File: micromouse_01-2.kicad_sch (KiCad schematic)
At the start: 50 parts, among them IC6 PCA9632TK,118, J1 Conn_01x02, M3 Fan_Motor, Q1 MCM3400A-TP, Q2 MCM3400A-TP, Q3 MCM3400A-TP, Q4 SSM6J808R_LXHF, SW1 SSSS810701, U1 SMT-0440-S-R, U2 LBR-127HLD, U3 LBR-127HLD, U4 LBR-127HLD, U5 LBR-127HLD, U6 LXDC55FAAA-203

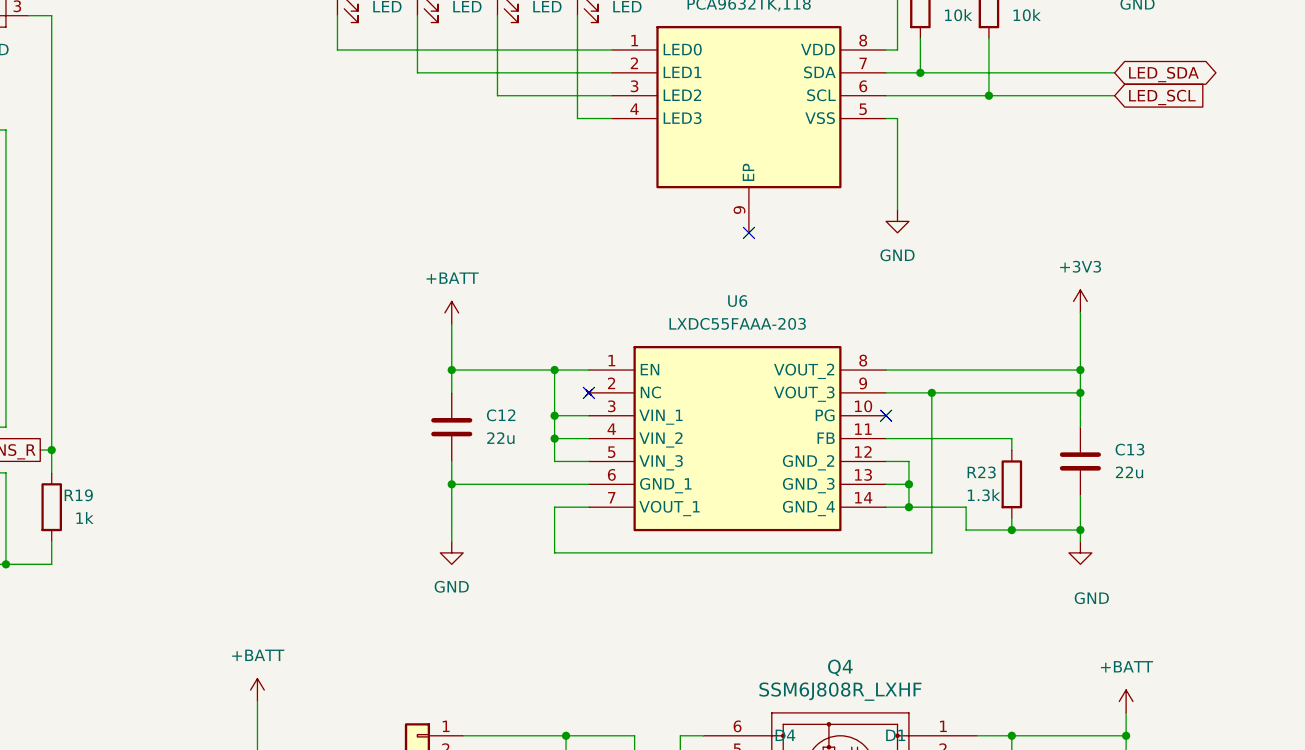
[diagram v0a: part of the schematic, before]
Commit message: [add]LED追加
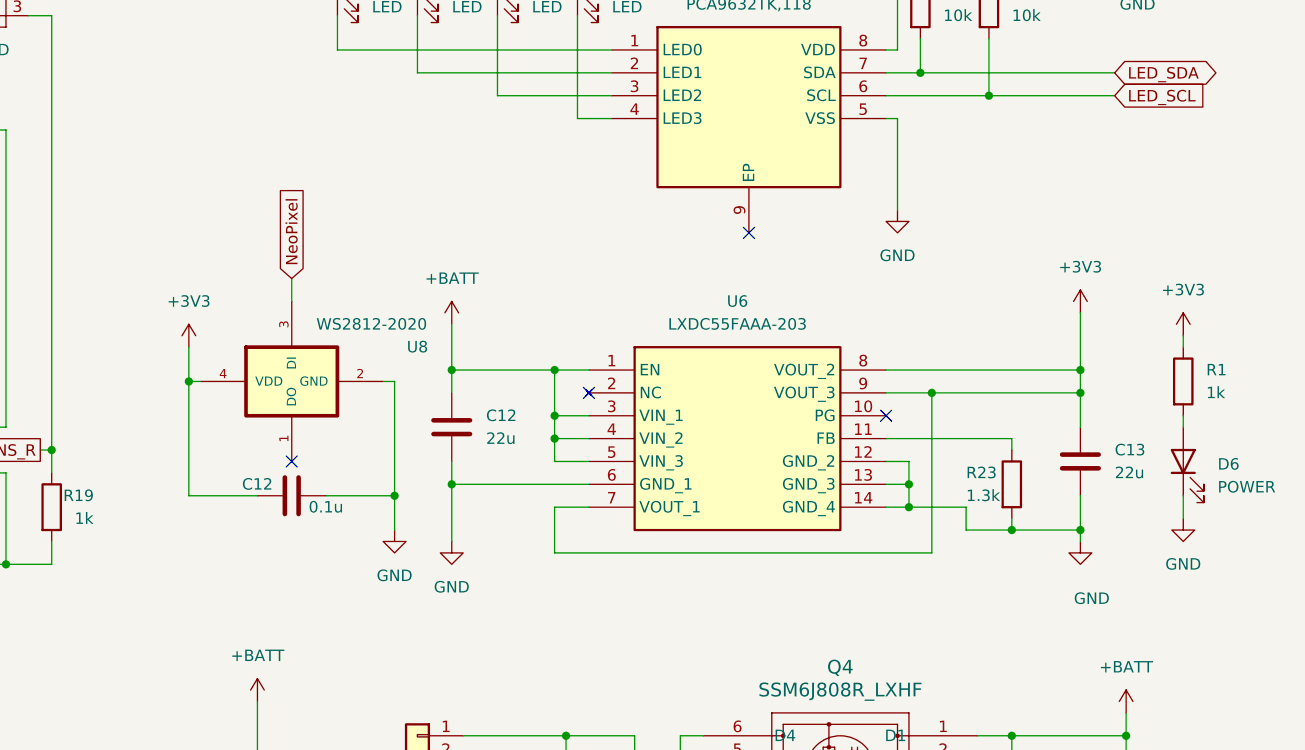
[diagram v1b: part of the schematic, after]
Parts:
- added C12: 0.1u, Capacitor_SMD:C_0402_1005Metric, symbol Device:C
- added D6: POWER, LED_SMD:LED_0402_1005Metric, symbol Device:LED
- added R1: 1k, Resistor_SMD:R_0402_1005Metric, symbol Device:R
- added U8: WS2812-2020, footprints:LED_WS2812-2020, symbol WS2812-2020:WS2812-2020
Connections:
- net +3V3: now also C12.1, R1.1, U8.4 (VDD)
- net GND: now also C12.2, D6.1 (K), U8.2 (GND)
- new net: D6.2 (A), R1.2
- new net NeoPixel: U8.3 (DI)
- no-connect marks 4 -> 5
